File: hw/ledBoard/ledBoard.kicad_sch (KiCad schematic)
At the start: 36 parts, among them J1 Conn_01x13_Socket, J2 Conn_01x13_Socket, J6 726386-2, J7 726386-2, Q1 NMOS, Q2 NMOS, U1 INA180A1, U4 LM5148RGYR

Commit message: hw - ledBoard
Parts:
- removed C21: 470nF, Capacitor_SMD:C_0805_2012Metric_Pad1.18x1.45mm_HandSolder, symbol Device:C
- removed C22, C23: 100nF, Capacitor_SMD:C_0805_2012Metric_Pad1.18x1.45mm_HandSolder, symbol Device:C
- removed C24: 4.7uF, Capacitor_SMD:C_0805_2012Metric_Pad1.18x1.45mm_HandSolder, symbol Device:C
- removed C25: 22p, Capacitor_SMD:C_0805_2012Metric_Pad1.18x1.45mm_HandSolder, symbol Device:C
- removed C26: 10uF, Capacitor_SMD:C_1210_3225Metric_Pad1.33x2.70mm_HandSolder, symbol Device:C
- removed C27: 2.7nF, Capacitor_SMD:C_0805_2012Metric_Pad1.18x1.45mm_HandSolder, symbol Device:C
- removed D1: 1N4448, Diode_SMD:D_SOD-523, symbol Diode:1N4448
- removed J2: Conn_01x13_Socket, Connector_PinSocket_2.54mm:PinSocket_1x13_P2.54mm_Vertical, symbol Connector:Conn_01x13_Socket
- removed J6, J7: 726386-2, 726386-2, symbol FASTON:726386-2
- removed NT2: NetTie_2, NetTie:NetTie-2_SMD_Pad0.5mm, symbol Device:NetTie_2
- removed Q1, Q2: NMOS, NMOS-CSD18514:DQJ0008A, symbol NMOS-CSD18514:CSD18514Q5A
- removed Rt1: 35.7k, Resistor_SMD:R_0805_2012Metric_Pad1.20x1.40mm_HandSolder, symbol Device:R
- removed U1: INA180A1, Package_TO_SOT_SMD:SOT-23-5, symbol Amplifier_Current:INA180A1
- removed U4: LM5148RGYR, LM5148:VQFN24_RGY_TEX, symbol LM5148:LM5148RGYR
- added C1: 470nF, Capacitor_SMD:C_0805_2012Metric_Pad1.18x1.45mm_HandSolder, symbol Device:C
- added C19, C20, C4, C5: 0.01uF, Capacitor_SMD:C_0805_2012Metric_Pad1.18x1.45mm_HandSolder, symbol Device:C
- added C2, C3: 10uF, Capacitor_SMD:C_1210_3225Metric_Pad1.33x2.70mm_HandSolder, symbol Device:C
- added C6, C7: C, Capacitor_SMD:C_0805_2012Metric_Pad1.18x1.45mm_HandSolder, symbol Device:C
- added C8, C9: 47uF, Capacitor_SMD:C_1210_3225Metric_Pad1.33x2.70mm_HandSolder, symbol Device:C
- added D1, D3: STPS3L40UF, SODFL5436X110N, symbol STPS3L40:STPS3L40UF
- added D2, D4: D, Diode_SMD:D_SOD-523, symbol Device:D
- added IC1, IC2: L7986A, SOIC127P600X170-9N, symbol L7986A:L7986A
- added J2, J3: Conn_01x02, Connector_JST:JST_XH_B2B-XH-A_1x02_P2.50mm_Vertical, symbol Connector_Generic:Conn_01x02
- added J5, J6, J9: Conn_01x03_Socket, Connector_PinSocket_2.54mm:PinSocket_1x03_P2.54mm_Vertical, symbol Connector:Conn_01x03_Socket
- added J8: Conn_01x05_Socket, Connector_PinSocket_2.54mm:PinSocket_1x05_P2.54mm_Vertical, symbol Connector:Conn_01x05_Socket
- added L2: L, Inductor_SMD:L_Bourns-SRN8040_8x8.15mm, symbol Device:L
- added R10, R11, R2: R, Resistor_SMD:R_0805_2012Metric_Pad1.20x1.40mm_HandSolder, symbol Device:R
- added R12: 10m, Resistor_SMD:R_0815_2038Metric_Pad1.20x4.05mm_HandSolder, symbol Device:R
- added U1, U2: INA180A4, Package_TO_SOT_SMD:SOT-23-5, symbol Amplifier_Current:INA180A4
- C12: value 0.01uF -> 470nF
- C13, C14: value 0.01uF -> C
- C15: value 10uF -> 47uF
- C18: value 0.01uF -> 47uF; footprint Capacitor_SMD:C_0805_2012Metric_Pad1.18x1.45mm_HandSolder -> Capacitor_SMD:C_1210_3225Metric_Pad1.33x2.70mm_HandSolder
- J1: value Conn_01x13_Socket -> Conn_02x11_Socket; footprint Connector_PinSocket_2.54mm:PinSocket_1x13_P2.54mm_Vertical -> Library:LedBoardPinHeader; symbol Connector:Conn_01x13_Socket -> Connector_Generic:Conn_02x11_Odd_Even
- L1: value 3.6uH -> L
- R1: value 22.5k -> R
- R3: value 10m -> R; footprint Resistor_SMD:R_0815_2038Metric_Pad1.20x4.05mm_HandSolder -> Resistor_SMD:R_0805_2012Metric_Pad1.20x1.40mm_HandSolder
- R4: value 41.2k -> R
- R5: value 10k -> 100k; now fitted
- R6: value 100k -> 10m; footprint Resistor_SMD:R_0805_2012Metric_Pad1.20x1.40mm_HandSolder -> Resistor_SMD:R_0815_2038Metric_Pad1.20x4.05mm_HandSolder
- R7, R9: value 10k -> R
- R8: value 140k -> 100k
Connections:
- net 24V: now also C1.1, C2.1, C3.1, C4.1, C5.1, IC1.8 (VCC), IC2.8 (VCC), J9.1 (Pin_1), J9.2 (Pin_2), J9.3 (Pin_3); no longer C13.1, C14.1, C15.1, C18.1
- net 5.2V: now also J1.3 (Pin_3), J1.4 (Pin_4); no longer J1.1 (Pin_1), J1.2 (Pin_2)
- net GND: now also J1.1 (Pin_1), J1.2 (Pin_2), R5.2, R8.2, C1.2, C19.2, C2.2, C20.2, C3.2, C4.2, C5.2, C8.2, C9.2, D1.2 (A), D3.2 (A), IC1.7 (GND), IC1.9 (EP), IC2.7 (GND), IC2.9 (EP), J2.2 (Pin_2), J3.2 (Pin_2), J6.1 (Pin_1), J6.2 (Pin_2), J6.3 (Pin_3), J8.3 (Pin_3), R10.2, R2.2, U1.2 (GND), U2.2 (GND); no longer C13.2, C14.2, J1.3 (Pin_3)
- net ICSP_CLK: now also J8.5 (Pin_5)
- net ICSP_DAT: now also J8.4 (Pin_4)
- net RA0: now also J1.8 (Pin_8), R8.1, IC2.3 (EN); no longer J1.6 (Pin_6), R6.2
- net RA1: now also J1.10 (Pin_10), D4.2 (A); no longer J1.7 (Pin_7)
- net RA2: now also J1.12 (Pin_12), R5.1, IC1.3 (EN); no longer J1.8 (Pin_8)
- net RA3: now also J1.14 (Pin_14), D2.2 (A); no longer J1.9 (Pin_9)
- net RA4: now also J1.16 (Pin_16); no longer J1.10 (Pin_10)
- net RA5: now also J1.18 (Pin_18); no longer J1.11 (Pin_11)
- net RA6: now also J1.20 (Pin_20); no longer J1.12 (Pin_12)
- net RA7: now also J1.22 (Pin_22); no longer J1.13 (Pin_13)
- net RC0: now also J1.15 (Pin_15)
- net RC1: now also J1.17 (Pin_17)
- net RC2: now also J1.19 (Pin_19)
- net RC3: now also J1.21 (Pin_21)
- net RC4: now also J1.13 (Pin_13)
- net RC5: now also J1.11 (Pin_11)
- net RC6: now also J1.9 (Pin_9)
- net RC7: now also J1.7 (Pin_7)
- net VDD: now also J1.6 (Pin_6), C19.1, C20.1, J8.2 (Pin_2), U1.5 (V+), U2.5 (V+); no longer J1.4 (Pin_4), R6.1
- net ~{MCLR}: now also J8.1 (Pin_1)
- net at R1.2: now also R3.1, R4.1, C7.2, IC1.5 (FB), R2.1
- net at R9.2: now also C13.2, R7.1, IC2.5 (FB), R10.1, R11.1; no longer R5.1
- net at L1.2: now also D3.1 (K), IC1.1 (OUT)
- net at R4.2: now also D2.1 (K)
- net GNDA: no longer names the net of R7.2
- net GNDA: now also C14.2; no longer R4.1
- net ISNS+: no longer names the net of R3.2
- net ISNS+: now also C6.2; no longer L1.1
- removed net LED_OUT: C10.1, C11.1, C16.1, C17.1, R3.1, R8.1
- net VDDA: no longer names the net of R9.1
- net VDDA: now also C15.1, C16.1, C17.1, C18.1, L2.1, R12.2, U2.3 (+)
- new net: C13.1, C14.1, IC2.4 (COMP)
- new net: C6.1, C7.1, IC1.4 (COMP)
- new net: C10.1, C11.1, C8.1, C9.1, L1.1, R1.1, R6.2, U1.3 (+)
- new net: D4.1 (K), R11.2
- new net: D1.1 (K), IC2.1 (OUT), L2.2
- new net LED_OUT_0: J2.1 (Pin_1), R6.1, U1.4 (-)
- new net LED_OUT_1: J3.1 (Pin_1), R12.1, U2.4 (-)
- new net RB0: J5.1 (Pin_1), U2.1
- new net RB1: J5.2 (Pin_2), U1.1
- new net RB5: J5.3 (Pin_3)
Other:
- note removed: "(Datasheet sec. 8.3.8)"
- note removed: "41.2 kΩ => Primary controller Spread spectrum: ON Dual phase: Disabled (Datasheet sec. 8.3.15)"
- note removed: "For external compensation"
- note removed: "Internal compensation (Datasheet sec. 8.3.10)"
- note removed: "Output from buck"
- note removed: "f_switch[kHz]=10^6/(45*Rt[kOhm]+53) f_switch = 602.59 kHz (Datasheet sec. 8.3.5)"

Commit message: hw - ledboard, compensation
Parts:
- added C21, C22: C, Capacitor_SMD:C_0805_2012Metric_Pad1.18x1.45mm_HandSolder, symbol Device:C
- added R13, R14: R, Resistor_SMD:R_0805_2012Metric_Pad1.20x1.40mm_HandSolder, symbol Device:R
- R1, R9: value R -> 190k
- R10, R2: value R -> 10k
- R11, R4: value R -> 127k
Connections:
- net at C15.1, C16.1, C17.1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: now also C21.1
- net at C13.2, IC2.5 (FB), R10.1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: now also R13.2
- net at C7.2, IC1.5 (FB), R1.2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: now also R14.2
- net at C10.1, C11.1, C8.1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: now also C22.1
- new net: C21.2, R13.1
- new net: C22.2, R14.1
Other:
- moved on the sheet: R1, R9

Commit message: hw - led board redesign
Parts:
- removed C1, C12: 470nF, Capacitor_SMD:C_0805_2012Metric_Pad1.18x1.45mm_HandSolder, symbol Device:C
- removed C11, C18: 47uF, Capacitor_SMD:C_1210_3225Metric_Pad1.33x2.70mm_HandSolder, symbol Device:C
- removed C21, C22: C, Capacitor_SMD:C_0805_2012Metric_Pad1.18x1.45mm_HandSolder, symbol Device:C
- removed D1, D3: STPS3L40UF, SODFL5436X110N, symbol STPS3L40:STPS3L40UF
- removed IC1, IC2: L7986A, SOIC127P600X170-9N, symbol L7986A:L7986A
- removed R13, R14: R, Resistor_SMD:R_0805_2012Metric_Pad1.20x1.40mm_HandSolder, symbol Device:R
- added C23, C24: 100nF, Capacitor_SMD:C_0805_2012Metric_Pad1.18x1.45mm_HandSolder, symbol Device:C
- added U3, U4: AP63356Q, Library:V-DFN3020-13, symbol buck-lib:AP63356Q
- C10, C15, C16, C17, C8, C9: value 47uF -> 22uF; footprint Capacitor_SMD:C_1210_3225Metric_Pad1.33x2.70mm_HandSolder -> Capacitor_SMD:C_0805_2012Metric_Pad1.18x1.45mm_HandSolder
- C13, C7: value C -> 100nF
- C14, C6: value C -> 6.8nF
- C19, C20: value 0.01uF -> 100nF
- C4, C5: value 0.01uF -> 10nF
- D2, D4: value D -> RB501SM
- L1, L2: value L -> 10uH; footprint Inductor_SMD:L_Bourns-SRN8040_8x8.15mm -> Inductor_SMD:L_Changjiang_FNR6045S
- R1, R9: value 190k -> 140k
- R11, R4: value 127k -> 100k
- R3, R7: value R -> 47k
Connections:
- net 24V: now also U3.1 (VIN), U4.1 (VIN)
- net GND: now also C13.1, C14.1, C6.1, C7.1, U3.8 (GND), U4.8 (GND)
- net RA0: now also U4.2 (EN)
- net RA2: now also U3.2 (EN)
- net RA4: now also U3.5 (PG)
- net RB5: now also U4.5 (PG)
- net at R10.1, R11.1, R9.2: now also U4.3 (FB); no longer C13.2, R7.1
- net at L1.2: now also C24.2, U3.9 (SW)
- net at R1.2, R2.1, R4.1: now also U3.3 (FB); no longer C7.2, R3.1
- net at L2.2: now also C23.2, U4.9 (SW)
- new net: C13.2, R7.1, U4.4 (COMP)
- new net: C7.2, R3.1, U3.4 (COMP)
- new net: C23.1, U4.6 (BST)
- new net: C24.1, U3.6 (BST)
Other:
- moved on the sheet: C13, C14, C2, C3, C4, C5, C6, C7, D2, D4, J8, J9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

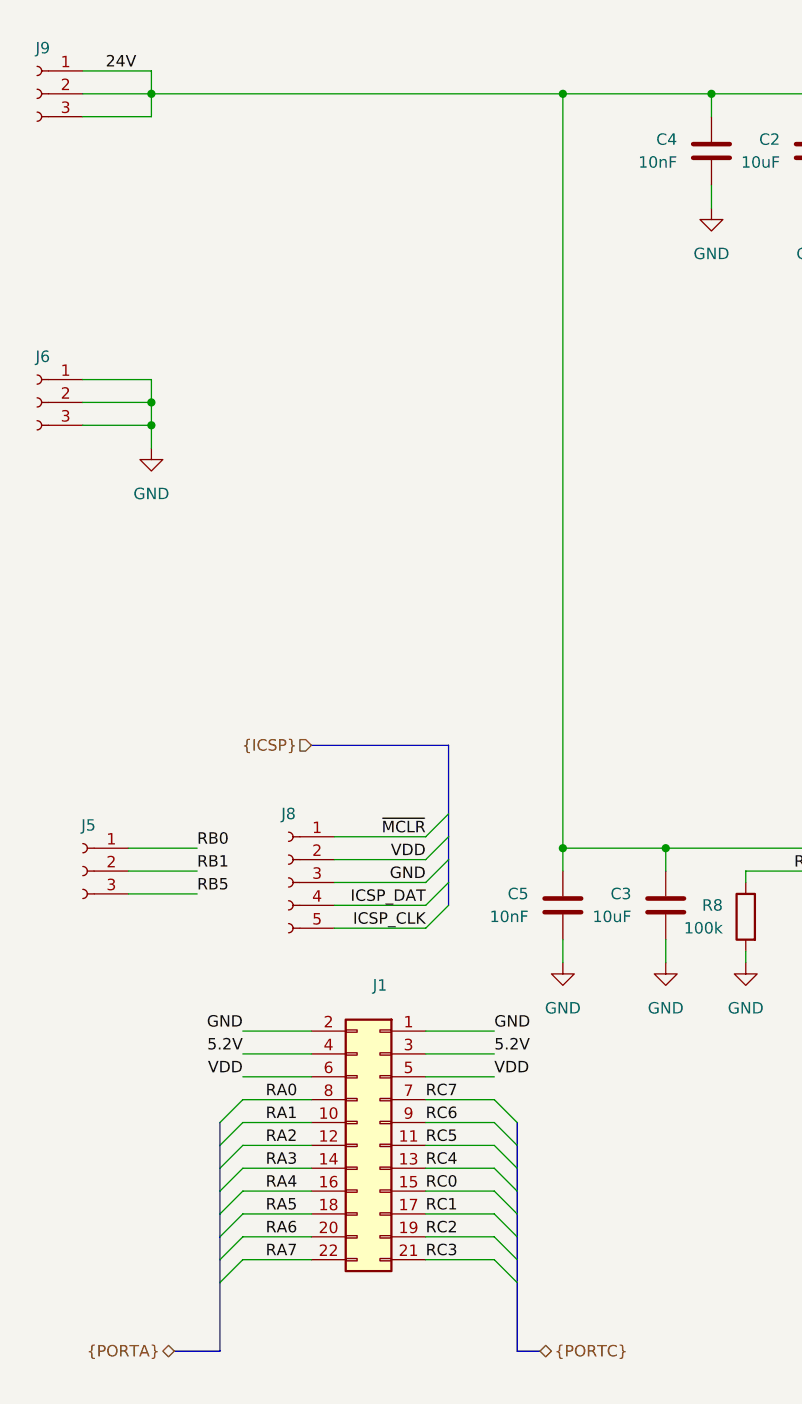
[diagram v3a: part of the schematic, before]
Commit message: text - periferie, obrazky hw - schemata
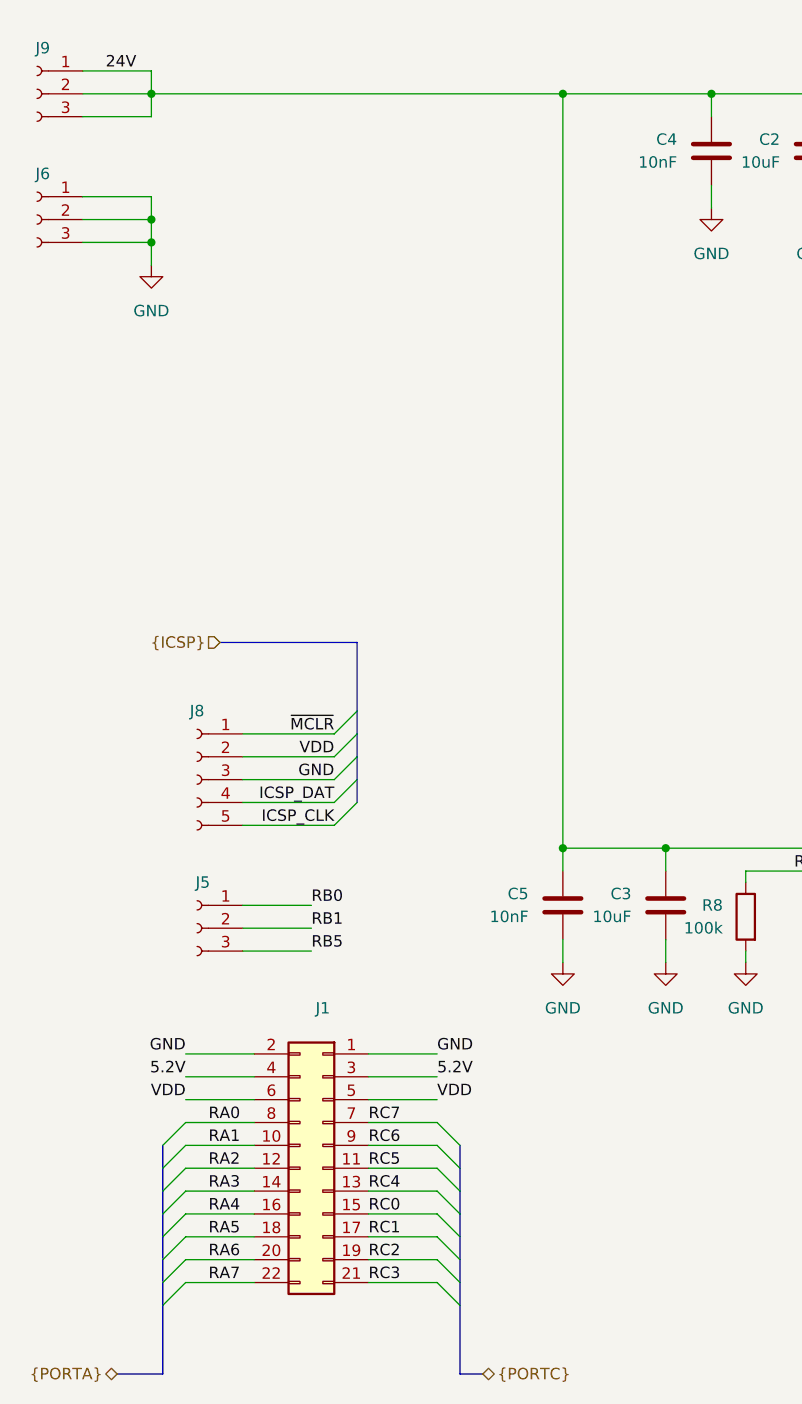
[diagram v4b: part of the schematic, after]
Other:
- moved on the sheet: J1, J5, J6, J8
